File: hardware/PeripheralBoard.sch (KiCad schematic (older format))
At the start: 20 parts, among them J1 PARAM1_CV, J2 PARAM2_CV, J3 CLK/TRG, J4 DITTO, J5 OUT1, J6 OUT2, J7 B1_HDR_LEFT, J8 B1_HDR_RIGHT

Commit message: [JNTUB-HW] JNTUB Hardware Revision 0.2
* Add resistor to drain C12 (PWM filter cap)
* Add optional parallel resistor to PWM filter
  * selectable by jumper
  * increases the cutoff frequency to audio range
* Add resistor between 5V and MCU RESET to allow for ISP
* Move a few resistors to Board 1
* Add ISP programming headers!
* Change all resistors and diodes to standing
* Shorten pin headers that connect Boards 1 and 2
* Ditch ground pour on Board 1 in favor of direct traces
* Move CV 1 and CV 2 jacks down a bit
* Slightly adjust LED positions
* Adjust front panel to match moved components
* Tweak design of front panel
* Fix up some 3D models
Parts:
- added R17: 330k, Resistors_THT:R_Axial_DIN0207_L6.3mm_D2.5mm_P2.54mm_Vertical, symbol Device:R
- added R21, R29: R_lim, Resistors_THT:R_Axial_DIN0207_L6.3mm_D2.5mm_P2.54mm_Vertical, symbol Device:R
- D6: value IN_LED -> CLK_LED
- D7: value OUT_LED+ -> LED_POS
- D8: value OUT_LED- -> LED_NEG
- J1, J2, J5, J6: footprint SDIY:PJ301M-12 -> SDIY:PJ301M-12_Thonkiconn
- J3, J4: footprint SDIY:PJ301M-12 -> SDIY:PJ301M-12_Thonkiconn_NoGround; symbol SDIY:JACK_MONO -> SDIY:JACK_MONO_NoRing
- J7, J8: footprint Pin_Headers:Pin_Header_Straight_1x09_Pitch2.54mm -> Pin_Headers:Pin_Header_Straight_1x07_Pitch2.54mm; symbol Connector:Conn_01x09_Male -> Connector:Conn_01x07_Male
- R1, R3, R7, R9: footprint SDIY:R_Axial_DIN0204_L3.6mm_D1.6mm_P5.08mm_Horizontal -> Resistors_THT:R_Axial_DIN0207_L6.3mm_D2.5mm_P2.54mm_Vertical
- R15: value R_out -> R_lim; footprint SDIY:R_Axial_DIN0204_L3.6mm_D1.6mm_P5.08mm_Horizontal -> Resistors_THT:R_Axial_DIN0207_L6.3mm_D2.5mm_P2.54mm_Vertical
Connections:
- net CLK_TRG: now also J8.6 (Pin_6), R15.1, R17.2; no longer J8.8 (Pin_8), R15.2
- net GNDREF: now also R17.1, R29.1; no longer J3.1, J4.1, J7.3 (Pin_3), J7.4 (Pin_4), J7.5 (Pin_5), J8.5 (Pin_5), J8.6 (Pin_6)
- net OUT: now also R21.2; no longer J5.3, J6.3
- net P1_AVG: now also J8.7 (Pin_7); no longer J7.9 (Pin_9)
- net P2_AVG: now also J7.7 (Pin_7), R1.1, R3.1; no longer J8.9 (Pin_9), R1.2, R3.2
- net P2_CV: now also R3.2; no longer R3.1
- net P2_POT: now also R1.2; no longer R1.1
- net P3_POT: now also J7.6 (Pin_6); no longer J7.8 (Pin_8)
- net at J1.2: now also J2.2, R29.2
- net DITTO: now reaches J4.3
- net DITTO: now also R15.2; no longer R15.1
- net IN_LED+ renamed CLK_LED
- net CLK_LED: now also J8.5 (Pin_5); no longer J8.7 (Pin_7)
- net OUT_LED+ renamed LED_POS
- net LED_POS: now also J7.5 (Pin_5); no longer J7.7 (Pin_7)
- net OUT_LED- renamed LED_NEG
- net LED_NEG: now also J7.4 (Pin_4); no longer J7.6 (Pin_6)
- new net OUT1: J5.3, J6.3, R21.1
- no-connect marks 6 -> 5
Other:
- note added: "Could really be -12V to +12V, but voltages are\nclamped before reaching the MCU so it’s fine\nto speak in terms of expected input."
- note added: "Ground pin shared\nwith J1"
- note added: "Ground pin shared\nwith J2"
- note added: "NOTES:\n\n- R_lim: Use 1k for 1/4W resistors. Use 2k for 1/8W resistors.\n\n- LED_NEG can be omitted from Board 1 but must be replaced\n with a regular switching diode to avoid damage to LED_POS."
- note removed: "*see note on MainBoard sheet"
- note removed: "Could really be -12V to +12V, but voltages are\nclamped before reaching the MCU so it’s fine\nto speak in terms of expectd input."
- note removed: "NOTES:\n\n- OUT_LED- can be omitted from the front\n panel but must be substituted for a regular\n switching diode to avoid damage to OUT_LED+."
- moved on the sheet: D7, D8, H1, J1, J2, R1, R15, R3, R7, R9

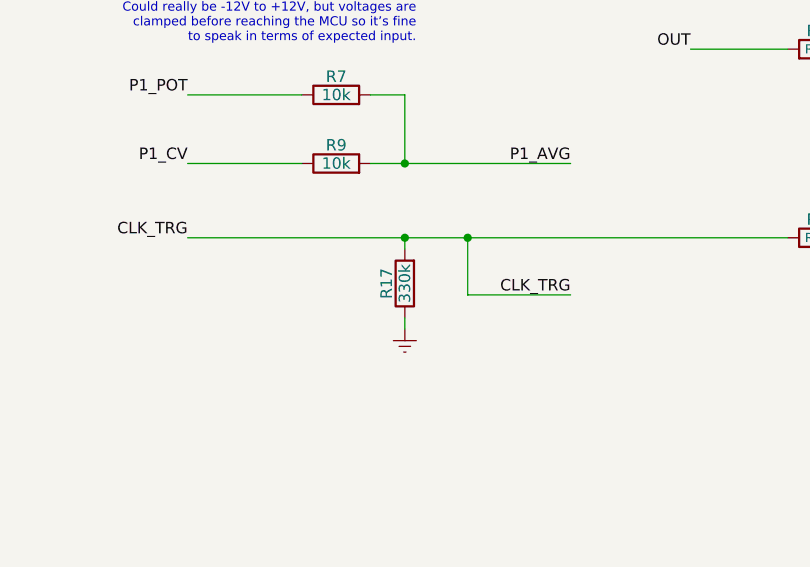
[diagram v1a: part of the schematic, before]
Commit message: [JNTUB-HW] Modify resistor values in schematic
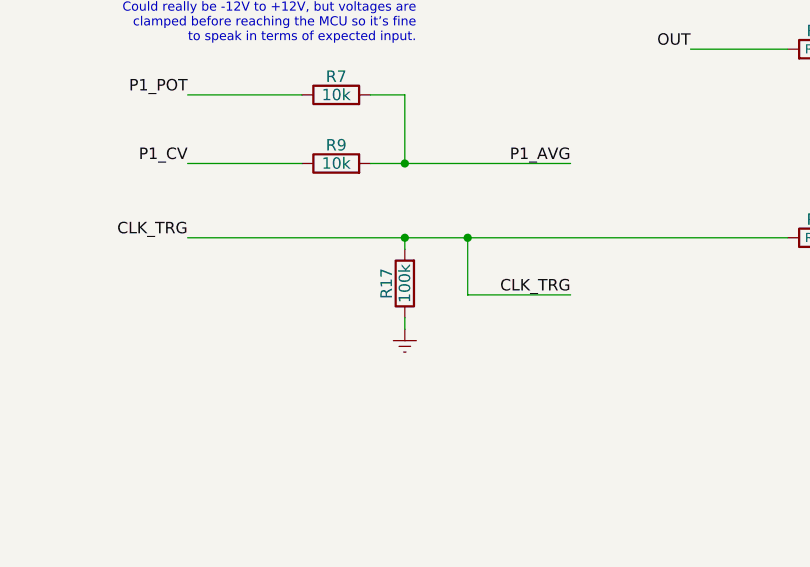
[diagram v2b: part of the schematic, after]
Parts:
- R17: value 330k -> 100k
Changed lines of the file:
@@
 AR Path="/5FE9B0F3/608FB227" Ref="R17"  Part="1"
 F 0 "R17" V 6580 2875 50  0000 C CNN
-F 1 "330k" V 6500 2875 50  0000 C CNN
+F 1 "100k" V 6500 2875 50  0000 C CNN
 F 2 "Resistors_THT:R_Axial_DIN0207_L6.3mm_D2.5mm_P2.54mm_Vertical" V 6430 2875 50  0001 C CNN
 F 3 "" H 6500 2875 50  0001 C CNN

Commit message: [JNTUB-HW] Some PCB and schematic updates
* Thicker silkscreen on diodes
* Give explicit values to some items
* Update potentiometer schematic symbols
* Fix some symbol names
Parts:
- D6: value CLK_LED -> LED
- D7: value LED_POS -> LED
- D8: value LED_NEG -> LED
- R1, R15, R17, R21, R29, R3, R7, R9: footprint Resistors_THT:R_Axial_DIN0207_L6.3mm_D2.5mm_P2.54mm_Vertical -> SDIY:R_Axial_DIN0207_L6.3mm_D2.5mm_P2.54mm_Vertical
- RV1, RV2, RV3: symbol JNTUB-rescue:POT -> Device:R_POT_MountingPin
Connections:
- net GNDREF: now also RV1.MP (MountPin), RV2.MP (MountPin), RV3.MP (MountPin)
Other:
- note added: "NOTES:\n\n- R15/R21: Use 1k for 1/4W resistors. Use 2k for 1/8W resistors.\n\n- D8 can be omitted from Board 1 but must be replaced\n with a regular switching diode to avoid damage to D7."
- note removed: "NOTES:\n\n- R_lim: Use 1k for 1/4W resistors. Use 2k for 1/8W resistors.\n\n- LED_NEG can be omitted from Board 1 but must be replaced\n with a regular switching diode to avoid damage to LED_POS."
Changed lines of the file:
@@
 $EndDescr
 $Comp
-L JNTUB-rescue:POT RV3
+L Device:R_POT_MountingPin RV3
 U 1 1 5FE9C832
 P 3250 1450
-F 0 "RV3" V 3075 1450 50  0000 C CNN
-F 1 "B100K" V 3150 1450 50  0000 C CNN
+F 0 "RV3" H 3007 1404 50  0000 R CNN
+F 1 "B100K" H 3007 1495 50  0000 R CNN
 F 2 "SDIY:Potentiometer_Alpha_9mm_WithGround" H 3250 1450 50  0001 C CNN
 F 3 "" H 3250 1450 50  0001 C CNN
@@
 $EndComp
 $Comp
-L JNTUB-rescue:POT RV2
+L Device:R_POT_MountingPin RV2
 U 1 1 5FE9C835
 P 3250 2450
-F 0 "RV2" V 3075 2450 50  0000 C CNN
-F 1 "B100K" V 3150 2450 50  0000 C CNN
+F 0 "RV2" H 3007 2404 50  0000 R CNN
+F 1 "B100K" H 3007 2495 50  0000 R CNN
 F 2 "SDIY:Potentiometer_Alpha_9mm_WithGround" H 3250 2450 50  0001 C CNN
 F 3 "" H 3250 2450 50  0001 C CNN
@@
 $EndComp
 $Comp
-L JNTUB-rescue:POT RV1
+L Device:R_POT_MountingPin RV1
 U 1 1 5FE9C839
 P 3250 3450
-F 0 "RV1" V 3075 3450 50  0000 C CNN
-F 1 "B100K" V 3150 3450 50  0000 C CNN
+F 0 "RV1" H 3007 3404 50  0000 R CNN
+F 1 "B100K" H 3007 3495 50  0000 R CNN
 F 2 "SDIY:Potentiometer_Alpha_9mm_WithGround" H 3250 3450 50  0001 C CNN
 F 3 "" H 3250 3450 50  0001 C CNN
@@
 P 3275 6350
 F 0 "D7" H 3275 6450 50  0000 C CNN
-F 1 "LED_POS" H 3275 6200 50  0000 C CNN
+F 1 "LED" H 3275 6200 50  0000 C CNN
 F 2 "LEDs:LED_D3.0mm" H 3275 6350 50  0001 C CNN
 F 3 "" H 3275 6350 50  0001 C CNN
@@
 P 3275 6650
 F 0 "D8" H 3275 6750 50  0000 C CNN
-F 1 "LED_NEG" H 3275 6500 50  0000 C CNN
+F 1 "LED" H 3275 6500 50  0000 C CNN
 F 2 "LEDs:LED_D3.0mm" H 3275 6650 50  0001 C CNN
 F 3 "" H 3275 6650 50  0001 C CNN
@@
 	3250 1200 3250 1300
 Wire Wire Line
-	3250 1600 3250 1700
-Wire Wire Line
 	3250 2200 3250 2300
 Wire Wire Line
@@
 P 3300 5600
 F 0 "D6" H 3300 5700 50  0000 C CNN
-F 1 "CLK_LED" H 3300 5450 50  0000 C CNN
+F 1 "LED" H 3300 5450 50  0000 C CNN
 F 2 "LEDs:LED_D3.0mm" H 3300 5600 50  0001 C CNN
 F 3 "" H 3300 5600 50  0001 C CNN
@@
 	1    3250 3700
 	-1   0    0    1
-$EndComp
-$Comp
-L Device:R R?
-U 1 1 61B5CD54
-P 8325 2675
-AR Path="/5FE97452/61B5CD54" Ref="R?"  Part="1"
-AR Path="/5FE9B0F3/61B5CD54" Ref="R15"  Part="1"
-F 0 "R15" V 8405 2675 50  0000 C CNN
-F 1 "R_lim" V 8325 2675 40  0000 C CNN
-F 2 "Resistors_THT:R_Axial_DIN0207_L6.3mm_D2.5mm_P2.54mm_Vertical" V 8255 2675 50  0001 C CNN
-F 3 "" H 8325 2675 50  0001 C CNN
-	1    8325 2675
-	0    -1   -1   0
 $EndComp
 Wire Wire Line
@@
 F 0 "R3" V 6305 1525 50  0000 C CNN
 F 1 "10k" V 6225 1525 50  0000 C CNN
-F 2 "Resistors_THT:R_Axial_DIN0207_L6.3mm_D2.5mm_P2.54mm_Vertical" V 6155 1525 50  0001 C CNN
+F 2 "SDIY:R_Axial_DIN0207_L6.3mm_D2.5mm_P2.54mm_Vertical" V 6155 1525 50  0001 C CNN
 F 3 "" H 6225 1525 50  0001 C CNN
 	1    6225 1525
@@
 F 0 "R1" V 6305 1225 50  0000 C CNN
 F 1 "10k" V 6225 1225 50  0000 C CNN
-F 2 "Resistors_THT:R_Axial_DIN0207_L6.3mm_D2.5mm_P2.54mm_Vertical" V 6155 1225 50  0001 C CNN
+F 2 "SDIY:R_Axial_DIN0207_L6.3mm_D2.5mm_P2.54mm_Vertical" V 6155 1225 50  0001 C CNN
 F 3 "" H 6225 1225 50  0001 C CNN
 	1    6225 1225
@@
 F 0 "R9" V 6280 2350 50  0000 C CNN
 F 1 "10k" V 6200 2350 50  0000 C CNN
-F 2 "Resistors_THT:R_Axial_DIN0207_L6.3mm_D2.5mm_P2.54mm_Vertical" V 6130 2350 50  0001 C CNN
+F 2 "SDIY:R_Axial_DIN0207_L6.3mm_D2.5mm_P2.54mm_Vertical" V 6130 2350 50  0001 C CNN
 F 3 "" H 6200 2350 50  0001 C CNN
 	1    6200 2350
@@
 F 0 "R7" V 6280 2050 50  0000 C CNN
 F 1 "10k" V 6200 2050 50  0000 C CNN
-F 2 "Resistors_THT:R_Axial_DIN0207_L6.3mm_D2.5mm_P2.54mm_Vertical" V 6130 2050 50  0001 C CNN
+F 2 "SDIY:R_Axial_DIN0207_L6.3mm_D2.5mm_P2.54mm_Vertical" V 6130 2050 50  0001 C CNN
 F 3 "" H 6200 2050 50  0001 C CNN
 	1    6200 2050
@@
 	8550 4675 9150 4675
 $Comp
-L Device:R R?
-U 1 1 608FB227
-P 6500 2875
-AR Path="/5FE97452/608FB227" Ref="R?"  Part="1"
-AR Path="/5FE9B0F3/608FB227" Ref="R17"  Part="1"
-F 0 "R17" V 6580 2875 50  0000 C CNN
-F 1 "100k" V 6500 2875 50  0000 C CNN
-F 2 "Resistors_THT:R_Axial_DIN0207_L6.3mm_D2.5mm_P2.54mm_Vertical" V 6430 2875 50  0001 C CNN
-F 3 "" H 6500 2875 50  0001 C CNN
-	1    6500 2875
-	-1   0    0    1
-$EndComp
-$Comp
 L power:GNDREF #PWR?
 U 1 1 608FB22D
@@
 CLK_TRG
 Connection ~ 6500 2675
-$Comp
-L Device:R R?
-U 1 1 60A49DEE
-P 8325 1850
-AR Path="/5FE97452/60A49DEE" Ref="R?"  Part="1"
-AR Path="/5FE9B0F3/60A49DEE" Ref="R21"  Part="1"
-F 0 "R21" V 8405 1850 50  0000 C CNN
-F 1 "R_lim" V 8325 1850 40  0000 C CNN
-F 2 "Resistors_THT:R_Axial_DIN0207_L6.3mm_D2.5mm_P2.54mm_Vertical" V 8255 1850 50  0001 C CNN
-F 3 "" H 8325 1850 50  0001 C CNN
-	1    8325 1850
-	0    1    -1   0
-$EndComp
 Text Label 7750 1850 2    50   ~ 0
 OUT
@@
 	8700 2050 9050 2050
 Connection ~ 8700 1850
-Text Notes 6700 6475 0    60   ~ 0
-NOTES:\n\n- R_lim: Use 1k for 1/4W resistors. Use 2k for 1/8W resistors.\n\n- LED_NEG can be omitted from Board 1 but must be replaced\n   with a regular switching diode to avoid damage to LED_POS.
 Text Label 4075 5350 2    50   ~ 0
 DITTO
@@
 F 0 "R29" V 3330 4725 50  0000 C CNN
 F 1 "R_lim" V 3250 4725 40  0000 C CNN
-F 2 "Resistors_THT:R_Axial_DIN0207_L6.3mm_D2.5mm_P2.54mm_Vertical" V 3180 4725 50  0001 C CNN
+F 2 "SDIY:R_Axial_DIN0207_L6.3mm_D2.5mm_P2.54mm_Vertical" V 3180 4725 50  0001 C CNN
 F 3 "" H 3250 4725 50  0001 C CNN
 	1    3250 4725
@@
 Text Notes 4325 5125 2    50   ~ 0
 Ground pin shared\nwith J2
+Wire Wire Line
+	3250 1600 3250 1700
+$Comp
+L power:GNDREF #PWR0119
+U 1 1 6021A020
+P 3050 1500
+F 0 "#PWR0119" H 3050 1250 50  0001 C CNN
+F 1 "GNDREF" H 3050 1350 50  0001 C CNN
+F 2 "" H 3050 1500 50  0001 C CNN
+F 3 "" H 3050 1500 50  0001 C CNN
+	1    3050 1500
+	1    0    0    -1
+$EndComp
+Wire Wire Line
+	3050 1450 3050 1500
+$Comp
+L power:GNDREF #PWR0123
+U 1 1 6021E886
+P 3050 2525
+F 0 "#PWR0123" H 3050 2275 50  0001 C CNN
+F 1 "GNDREF" H 3050 2375 50  0001 C CNN
+F 2 "" H 3050 2525 50  0001 C CNN
+F 3 "" H 3050 2525 50  0001 C CNN
+	1    3050 2525
+	1    0    0    -1
+$EndComp
+Wire Wire Line
+	3050 2525 3050 2450
+$Comp
+L power:GNDREF #PWR0124
+U 1 1 6022381F
+P 3050 3525
+F 0 "#PWR0124" H 3050 3275 50  0001 C CNN
+F 1 "GNDREF" H 3050 3375 50  0001 C CNN
+F 2 "" H 3050 3525 50  0001 C CNN
+F 3 "" H 3050 3525 50  0001 C CNN
+	1    3050 3525
+	1    0    0    -1
+$EndComp
+Wire Wire Line
+	3050 3525 3050 3450
+Text Notes 6700 6475 0    60   ~ 0
+NOTES:\n\n- R15/R21: Use 1k for 1/4W resistors. Use 2k for 1/8W resistors.\n\n- D8 can be omitted from Board 1 but must be replaced\n   with a regular switching diode to avoid damage to D7.
+$Comp
+L Device:R R?
+U 1 1 61B5CD54
+P 8325 2675
+AR Path="/5FE97452/61B5CD54" Ref="R?"  Part="1"
+AR Path="/5FE9B0F3/61B5CD54" Ref="R15"  Part="1"
+F 0 "R15" V 8405 2675 50  0000 C CNN
+F 1 "R_lim" V 8325 2675 40  0000 C CNN
+F 2 "SDIY:R_Axial_DIN0207_L6.3mm_D2.5mm_P2.54mm_Vertical" V 8255 2675 50  0001 C CNN
+F 3 "" H 8325 2675 50  0001 C CNN
+	1    8325 2675
+	0    -1   -1   0
+$EndComp
+$Comp
+L Device:R R?
+U 1 1 608FB227
+P 6500 2875
+AR Path="/5FE97452/608FB227" Ref="R?"  Part="1"
+AR Path="/5FE9B0F3/608FB227" Ref="R17"  Part="1"
+F 0 "R17" V 6580 2875 50  0000 C CNN
+F 1 "100k" V 6500 2875 50  0000 C CNN
+F 2 "SDIY:R_Axial_DIN0207_L6.3mm_D2.5mm_P2.54mm_Vertical" V 6430 2875 50  0001 C CNN
+F 3 "" H 6500 2875 50  0001 C CNN
+	1    6500 2875
+	-1   0    0    1
+$EndComp
+$Comp
+L Device:R R?
+U 1 1 60A49DEE
+P 8325 1850
+AR Path="/5FE97452/60A49DEE" Ref="R?"  Part="1"
+AR Path="/5FE9B0F3/60A49DEE" Ref="R21"  Part="1"
+F 0 "R21" V 8405 1850 50  0000 C CNN
+F 1 "R_lim" V 8325 1850 40  0000 C CNN
+F 2 "SDIY:R_Axial_DIN0207_L6.3mm_D2.5mm_P2.54mm_Vertical" V 8255 1850 50  0001 C CNN
+F 3 "" H 8325 1850 50  0001 C CNN
+	1    8325 1850
+	0    1    -1   0
+$EndComp
 $EndSCHEMATC
